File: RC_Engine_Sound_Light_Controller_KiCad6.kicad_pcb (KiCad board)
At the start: 2 copper layers, 70 x 39 mm, 36 parts, among them J1 RX, J10 RGB, J11 32, J12 CH1, J13 CH2, J14 CH3, J15 ESC, J16 CH4, J2 HeadL, J3 TailL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

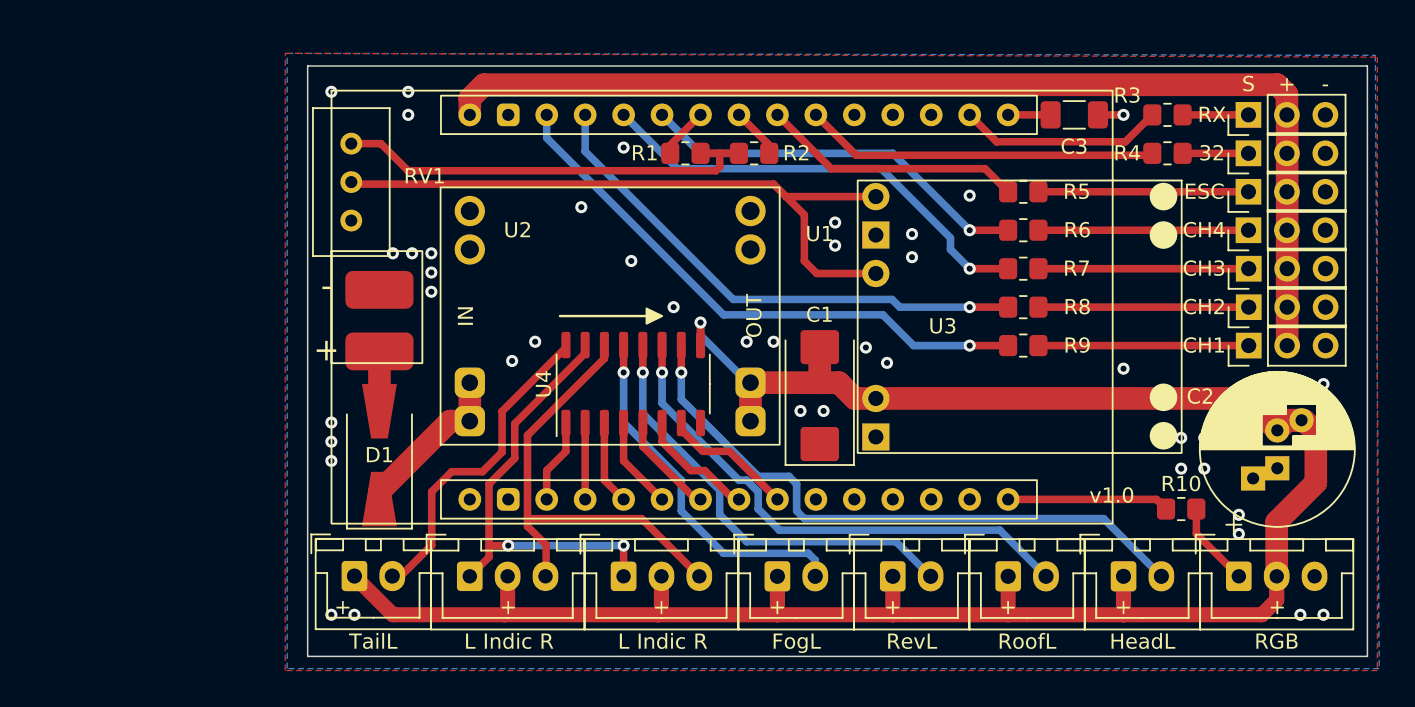
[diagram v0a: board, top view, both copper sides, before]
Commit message: Added RZ7886 to schematic
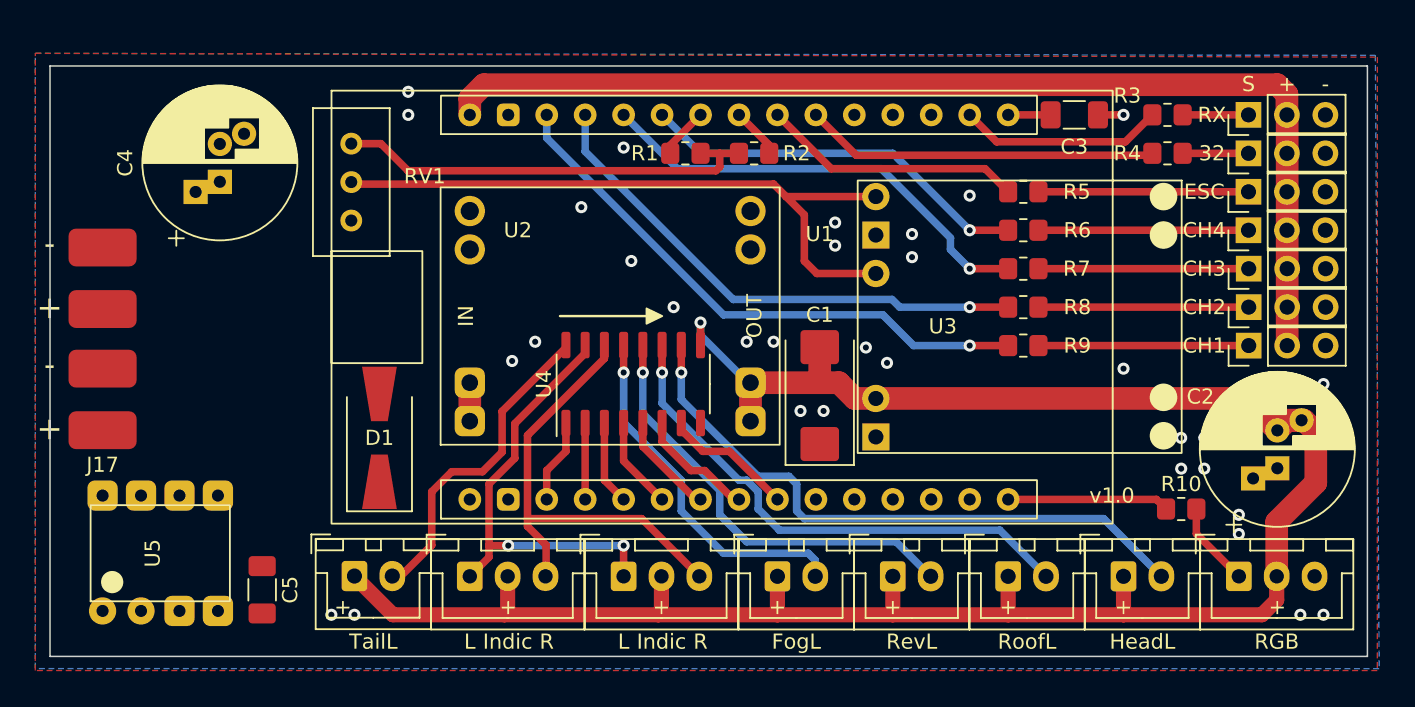
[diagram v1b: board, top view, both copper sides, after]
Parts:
- added C4: 470µF, Capacitor_THT:CP_Radial_D10.0mm_P2.50mm_P5.00mm, F.Cu at (76.2, 53.9)
- added C5: 100nF, Capacitor_SMD:C_1206_3216Metric_Pad1.33x1.80mm_HandSolder, F.Cu at (79.0, 80.9)
- added J17: Brushed Motor output, cf:InputPowerSolderPads, F.Cu at (68.5, 68.3)
- added U5: RZ7886, cf:RZ7886_DIP8, F.Cu at (72.3, 78.5)
- moved J8 18.5 mm to (68.5, 60.3)
- moved D1 1.14 mm to (86.7, 70.9)
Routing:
- net Net-(D1-Pad1): track 10.4 -> 2.54 mm
- net +12V: track 3.96 -> 0.00 mm
- net GND: vias 43 -> 34
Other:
- board size 70 x 39 mm -> 87 x 39 mm

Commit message: All but data lines routed
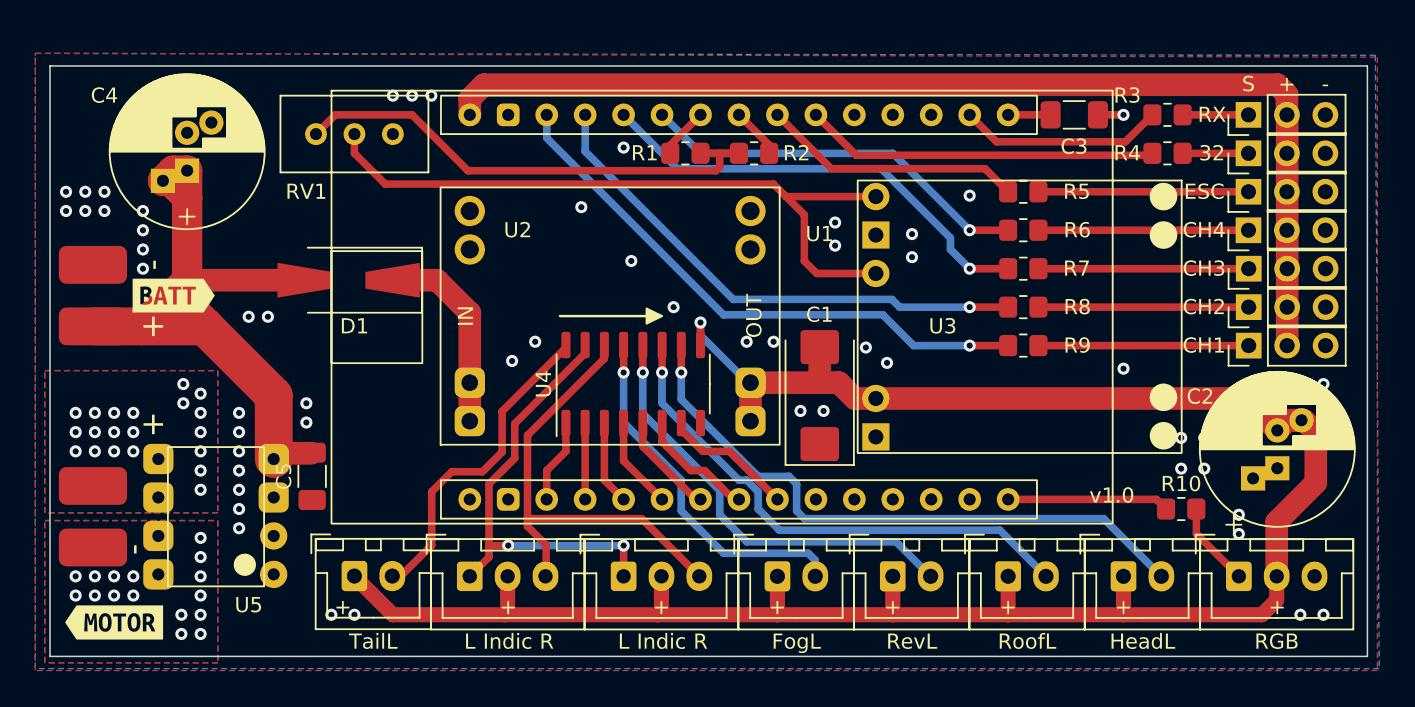
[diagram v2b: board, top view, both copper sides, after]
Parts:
- added kibuzzard-628752C5: G***, kibuzzard-628752C5, F.Cu at (73.2, 61.5)
- added kibuzzard-628752E8: G***, kibuzzard-628752E8, F.Cu at (69.2, 83.1)
- moved D1 10.6 mm to (84.7, 60.5), turned to 180 degrees
- moved C5 8.19 mm to (82.3, 73.4), turned to 90 degrees
- moved J17 7.77 mm to (67.8, 76.1)
- moved U5 4.40 mm to (75.9, 76.1), turned to 180 degrees
- moved RV1 2.41 mm to (82.5, 50.8), turned to 180 degrees
- moved C4 2.28 mm to (74.0, 53.2)
- moved J8 1.31 mm to (67.8, 61.5)
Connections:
- net Net-(D1-Pad1) renamed +10V
- net Net-(J12-Pad1) renamed /CH1
- net Net-(J13-Pad1) renamed /CH2
- net Net-(J15-Pad1) renamed /ESC
- net Net-(J17-Pad1) renamed /MOTOR_BO
- net Net-(J17-Pad2) renamed /MOTOR_FO
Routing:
- net +12V: track 0.00 -> 47.5 mm
- net +10V: track 2.54 -> 13.1 mm
- net Net-(R1-Pad2): track 28.6 -> 32.3 mm
- net Net-(RV1-Pad2): track 44.7 -> 46.7 mm
- net GND: vias 34 -> 56
- net /MOTOR_FO: vias 0 -> 15
- net /MOTOR_BO: vias 0 -> 12
- net (no net): vias 0 -> 9
- added copper zone on B.Cu, net /MOTOR_BO
- added copper zone on F.Cu, net /MOTOR_BO
- added copper zone on B.Cu, net /MOTOR_FO
- added copper zone on F.Cu, net /MOTOR_FO

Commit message: Minor corrections.
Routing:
- net /MOTOR_FO: vias 15 -> 20
- net /MOTOR_BO: vias 12 -> 16
- net (no net): vias 9 -> 0
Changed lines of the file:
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@@
       (net 10 "D18") (pinfunction "I7") (pintype "input"))
     (pad "8" smd roundrect (at -2.575 4.445 90) (size 1.75 0.6) (layers "F.Cu" "F.Paste" "F.Mask") (roundrect_rratio 0.25)
-      (net 2 "GND") (pinfunction "GND") (pintype "power_in"))
+      (net 2 "GND") (pinfunction "GND") (pintype "power_in") (zone_connect 2) (thermal_width 0.1) (thermal_gap 0.2))
     (pad "9" smd roundrect (at 2.575 4.445 90) (size 1.75 0.6) (layers "F.Cu" "F.Paste" "F.Mask") (roundrect_rratio 0.25)
       (net 3 "+5V") (pinfunction "COM") (pintype "passive"))
@@
     (effects (font (size 1 1) (thickness 0.15)))
   )
-  (via (at 70.485 71.755) (size 0.8) (drill 0.4) (layers "F.Cu" "B.Cu") (free) (net 0))
-  (via (at 70.485 70.485) (size 0.8) (drill 0.4) (layers "F.Cu" "B.Cu") (free) (net 0))
-  (via (at 73.787 67.31) (size 0.8) (drill 0.4) (layers "F.Cu" "B.Cu") (free) (net 0))
-  (via (at 73.787 68.58) (size 0.8) (drill 0.4) (layers "F.Cu" "B.Cu") (free) (net 0))
-  (via (at 73.66 83.82) (size 0.8) (drill 0.4) (layers "F.Cu" "B.Cu") (free) (net 0))
-  (via (at 73.66 82.55) (size 0.8) (drill 0.4) (layers "F.Cu" "B.Cu") (free) (net 0))
-  (via (at 70.485 80.01) (size 0.8) (drill 0.4) (layers "F.Cu" "B.Cu") (free) (net 0))
-  (via (at 70.485 69.215) (size 0.8) (drill 0.4) (layers "F.Cu" "B.Cu") (free) (net 0))
-  (via (at 70.485 81.28) (size 0.8) (drill 0.4) (layers "F.Cu" "B.Cu") (free) (net 0))
   (segment (start 139.795 52.07) (end 144.145 52.07) (width 0.5) (layer "F.Cu") (net 1))
   (segment (start 134.2013 49.53) (end 135.89 49.53) (width 0.5) (layer "F.Cu") (net 2))
@@
   (segment (start 90.551 60.452) (end 92.71 62.611) (width 1.5) (layer "F.Cu") (net 46))
   (segment (start 92.71 67.22) (end 92.71 69.76) (width 1.5) (layer "F.Cu") (net 46))
+  (via (at 70.485 71.755) (size 0.8) (drill 0.4) (layers "F.Cu" "B.Cu") (free) (net 47))
+  (via (at 70.485 70.485) (size 0.8) (drill 0.4) (layers "F.Cu" "B.Cu") (free) (net 47))
   (via (at 67.945 71.755) (size 0.8) (drill 0.4) (layers "F.Cu" "B.Cu") (free) (net 47))
   (via (at 66.675 69.215) (size 0.8) (drill 0.4) (layers "F.Cu" "B.Cu") (free) (net 47))
+  (via (at 73.787 67.31) (size 0.8) (drill 0.4) (layers "F.Cu" "B.Cu") (free) (net 47))
   (via (at 74.93 71.755) (size 0.8) (drill 0.4) (layers "F.Cu" "B.Cu") (free) (net 47))
   (via (at 74.93 69.215) (size 0.8) (drill 0.4) (layers "F.Cu" "B.Cu") (free) (net 47))
   (via (at 69.215 69.215) (size 0.8) (drill 0.4) (layers "F.Cu" "B.Cu") (free) (net 47))
+  (via (at 73.787 68.58) (size 0.8) (drill 0.4) (layers "F.Cu" "B.Cu") (free) (net 47))
   (via (at 66.675 70.485) (size 0.8) (drill 0.4) (layers "F.Cu" "B.Cu") (free) (net 47))
   (via (at 74.93 73.025) (size 0.8) (drill 0.4) (layers "F.Cu" "B.Cu") (free) (net 47))
@@
   (via (at 69.215 70.485) (size 0.8) (drill 0.4) (layers "F.Cu" "B.Cu") (free) (net 47))
   (via (at 69.215 71.755) (size 0.8) (drill 0.4) (layers "F.Cu" "B.Cu") (free) (net 47))
+  (via (at 70.485 69.215) (size 0.8) (drill 0.4) (layers "F.Cu" "B.Cu") (free) (net 47))
   (via (at 74.93 74.295) (size 0.8) (drill 0.4) (layers "F.Cu" "B.Cu") (free) (net 47))
   (via (at 66.675 81.28) (size 0.8) (drill 0.4) (layers "F.Cu" "B.Cu") (free) (net 48))
   (via (at 74.93 78.74) (size 0.8) (drill 0.4) (layers "F.Cu" "B.Cu") (free) (net 48))
+  (via (at 73.66 83.82) (size 0.8) (drill 0.4) (layers "F.Cu" "B.Cu") (free) (net 48))
   (via (at 67.945 81.28) (size 0.8) (drill 0.4) (layers "F.Cu" "B.Cu") (free) (net 48))
   (via (at 74.93 83.82) (size 0.8) (drill 0.4) (layers "F.Cu" "B.Cu") (free) (net 48))
   (via (at 66.675 80.01) (size 0.8) (drill 0.4) (layers "F.Cu" "B.Cu") (free) (net 48))
   (via (at 74.93 81.28) (size 0.8) (drill 0.4) (layers "F.Cu" "B.Cu") (free) (net 48))
+  (via (at 73.66 82.55) (size 0.8) (drill 0.4) (layers "F.Cu" "B.Cu") (free) (net 48))
   (via (at 74.93 82.55) (size 0.8) (drill 0.4) (layers "F.Cu" "B.Cu") (free) (net 48))
+  (via (at 70.485 80.01) (size 0.8) (drill 0.4) (layers "F.Cu" "B.Cu") (free) (net 48))
   (via (at 74.93 77.47) (size 0.8) (drill 0.4) (layers "F.Cu" "B.Cu") (free) (net 48))
   (via (at 69.215 80.01) (size 0.8) (drill 0.4) (layers "F.Cu" "B.Cu") (free) (net 48))
   (via (at 69.215 81.28) (size 0.8) (drill 0.4) (layers "F.Cu" "B.Cu") (free) (net 48))
   (via (at 67.945 80.01) (size 0.8) (drill 0.4) (layers "F.Cu" "B.Cu") (free) (net 48))
+  (via (at 70.485 81.28) (size 0.8) (drill 0.4) (layers "F.Cu" "B.Cu") (free) (net 48))
   (via (at 74.93 80.01) (size 0.8) (drill 0.4) (layers "F.Cu" "B.Cu") (free) (net 48))
   (segment (start 130.27 64.77) (end 144.16 64.77) (width 0.5) (layer "F.Cu") (net 49))
@@
     )
   )
-  (zone (net 2) (net_name "GND") (layer "F.Cu") (name "GND F") (hatch edge 0.508)
+  (zone (net 2) (net_name "GND") (layers F&B.Cu) (name "GND F") (hatch edge 0.508)
     (connect_pads (clearance 0.5))
     (min_thickness 0.7) (filled_areas_thickness no)
@@
       )
     )
-  )
-  (zone (net 2) (net_name "GND") (layer "B.Cu") (name "GND B") (hatch edge 0.508)
-    (connect_pads (clearance 0.5))
-    (min_thickness 0.7) (filled_areas_thickness no)
-    (fill yes (thermal_gap 0.5) (thermal_bridge_width 0.7) (smoothing fillet) (radius 1))
-    (polygon
-      (pts
-        (xy 152.777626 86.110092)
-        (xy 64.008091 86.105204)
-        (xy 64.009771 45.467401)
-        (xy 152.525306 45.599289)
-      )
-    )

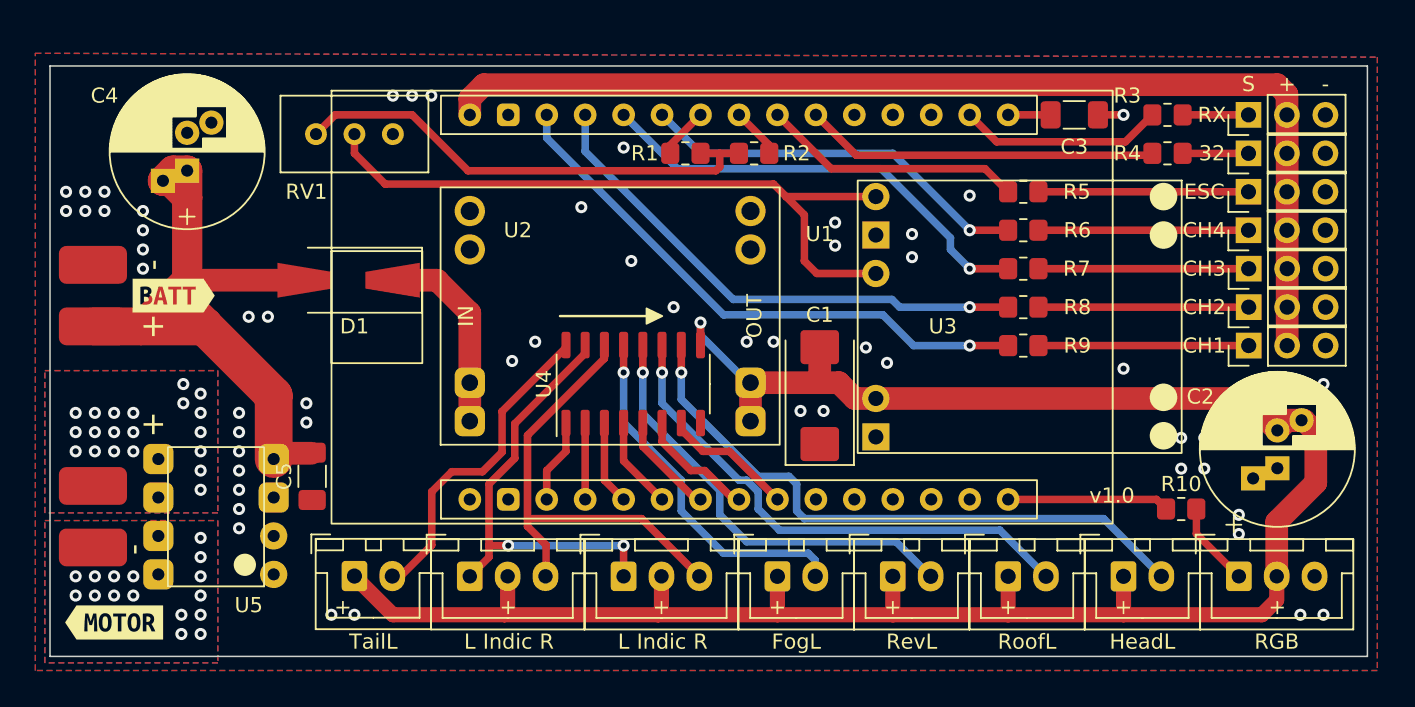
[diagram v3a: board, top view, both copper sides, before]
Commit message: Pins 32 and 33 connected to driver IC.
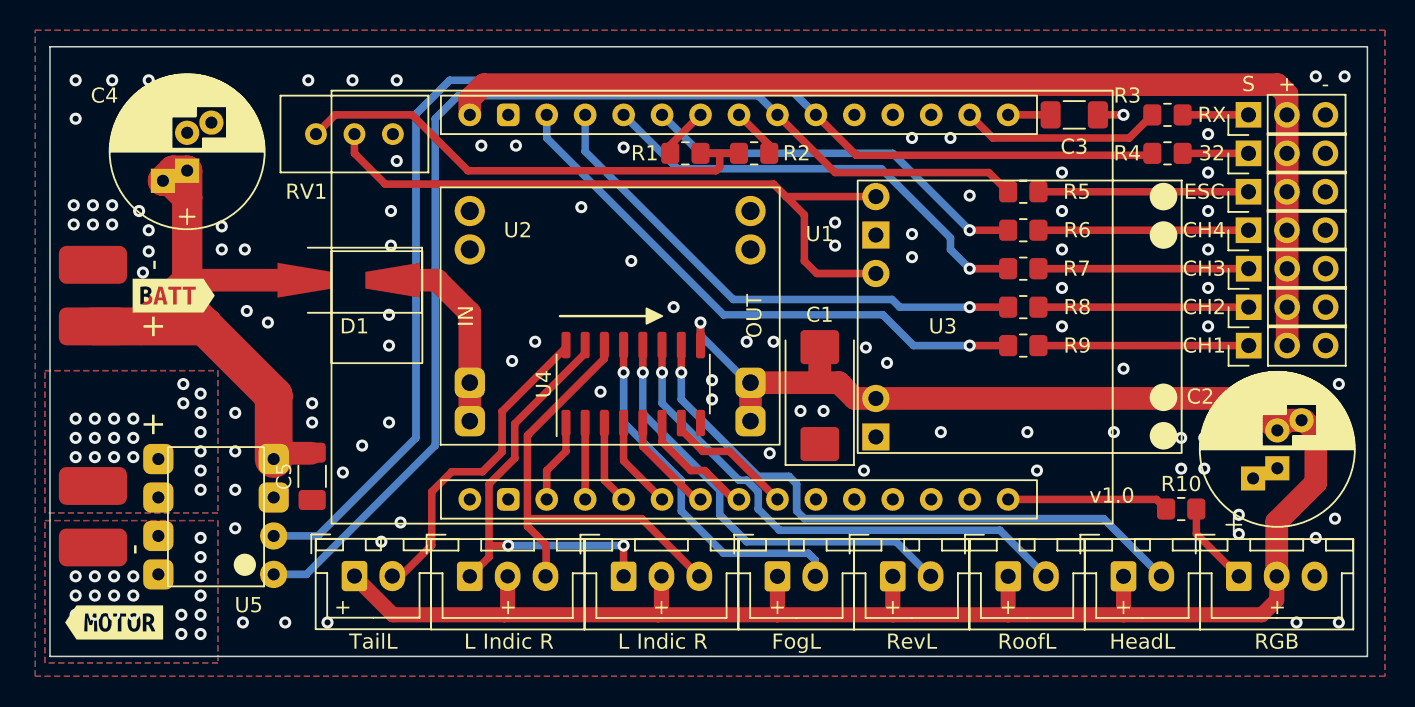
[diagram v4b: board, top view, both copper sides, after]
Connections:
- net Net-(J1-Pad1) renamed /RX
- net Net-(J10-Pad1) renamed /RGB
- net Net-(J11-Pad1) renamed /PIN_32
- net Net-(J14-Pad1) renamed /CH3
- net Net-(J16-Pad1) renamed /CH4
- net Net-(R1-Pad2) renamed /AUDIO_JOINT
- net Net-(RV1-Pad2) renamed /AUDIO_IN
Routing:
- net D32: track 23.2 -> 85.0 mm
- net D33: track 17.3 -> 76.9 mm
- net +12V: track 47.5 -> 46.9 mm
- net GND: vias 56 -> 99
- net /MOTOR_BO: vias 16 -> 20
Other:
- board size 87 x 39 mm -> 87 x 40.3 mm

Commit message: Added seconds tantal cap.
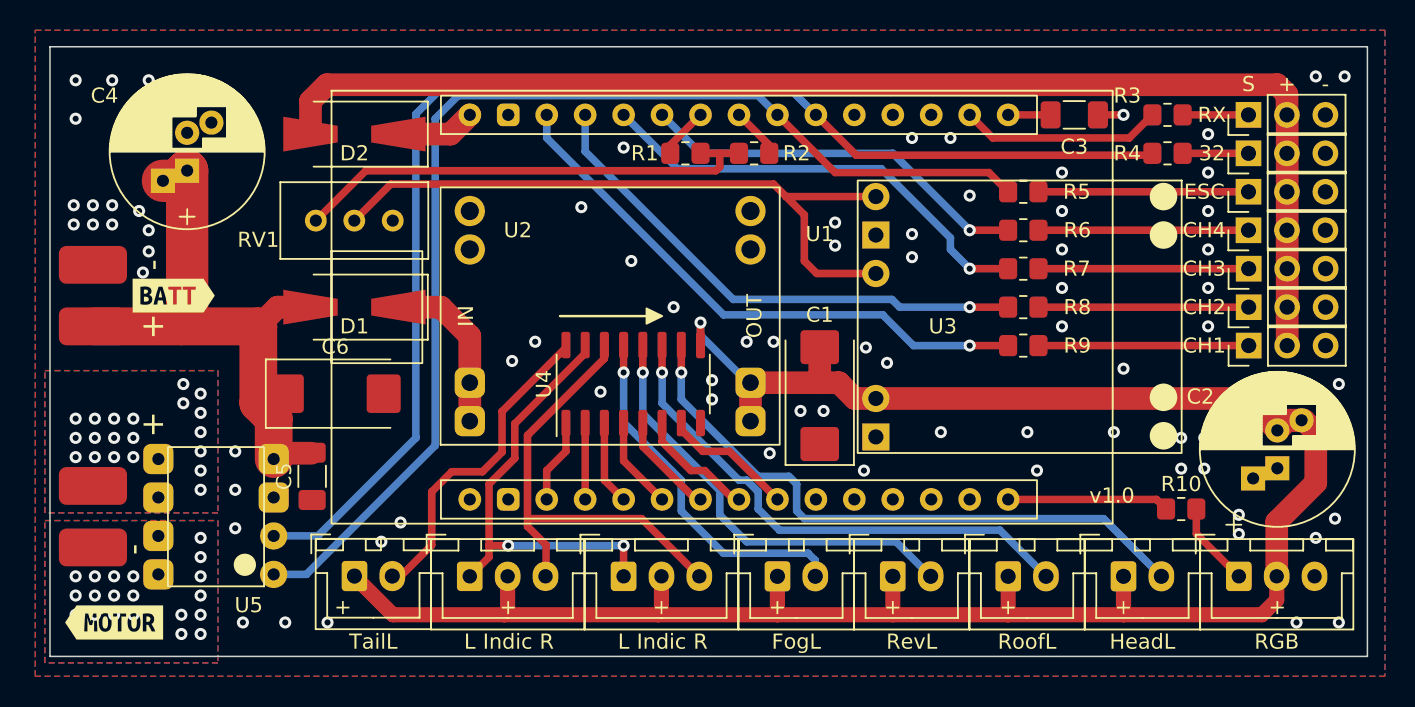
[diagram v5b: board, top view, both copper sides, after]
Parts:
- added C6: 330µF, Capacitor_Tantalum_SMD:CP_EIA-7343-30_AVX-N_Pad2.25x2.55mm_HandSolder, F.Cu at (83.8, 67.9)
- added D2: USB Supply Protection, Diode_SMD:D_SMA-SMB_Universal_Handsoldering, F.Cu at (85.1, 50.8)
- D1: value D_Schottky -> Polarity Protection
- moved RV1 5.72 mm to (82.5, 56.5)
- moved D1 1.82 mm to (85.1, 62.2)
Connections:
- U1 pad 30: VDD -> Net-(D2-Pad1)
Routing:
- net VDD: track 72.3 -> 84.0 mm
- net +12V: track 46.9 -> 38.5 mm
- net Net-(D2-Pad1): track 0.00 -> 5.25 mm
- net +10V: track 13.1 -> 11.1 mm
- net /AUDIO_IN: track 46.7 -> 45.6 mm
- net /AUDIO_JOINT: track 32.3 -> 31.6 mm
- net GND: vias 99 -> 78
